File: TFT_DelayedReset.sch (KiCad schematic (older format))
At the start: 14 parts, among them Q2 MMBT3904, U3 MCP601-xOT, U4 LM555xM, U5 MCP1416, U6 MCP1415

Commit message: Swapped LM555 with MIC1555
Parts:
- removed U4: LM555xM, Package_SO:SOIC-8_3.9x4.9mm_P1.27mm, symbol Timer:LM555xM
- added U4: MIC1555-YM5, Package_TO_SOT_SMD:SOT-23-5_HandSoldering, symbol MIC155x:MIC1555-YM5
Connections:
- wire segments 57 -> 54
- no-connect marks 1 -> 0
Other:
- moved on the sheet: U3
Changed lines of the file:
@@
 L Amplifier_Operational:MCP601-xOT U?
 U 1 1 5F17E98F
-P 2275 4125
+P 2275 3350
 AR Path="/5F02F4E9/5F17E98F" Ref="U?"  Part="1"
 AR Path="/5F02F4E9/5F1755C4/5F17E98F" Ref="U3"  Part="1"
-F 0 "U3" H 1800 4625 50  0000 L CNN
-F 1 "MCP601-xOT" H 1575 4500 50  0000 L CNN
-F 2 "Package_TO_SOT_SMD:SOT-23-5" H 2175 3925 50  0001 L CNN
-F 3 "http://ww1.microchip.com/downloads/en/DeviceDoc/21314g.pdf" H 2275 4325 50  0001 C CNN
-	1    2275 4125
-	1    0    0    -1
-$EndComp
-Wire Wire Line
-	2175 4425 2175 4475
-Text HLabel 2175 4475 3    50   Input ~ 0
-TFTRST_GND
-Wire Wire Line
-	2175 3825 2175 3450
-Text HLabel 2175 3450 1    50   Input ~ 0
-TFTRST_5V
-Wire Wire Line
-	1975 4025 1625 4025
-Wire Wire Line
-	1975 4225 1600 4225
-Wire Wire Line
-	1600 4225 1600 5200
-Wire Wire Line
-	1600 5200 2725 5200
-Wire Wire Line
-	2725 5200 2725 4125
-Wire Wire Line
-	2725 4125 2575 4125
-$Comp
-L Timer:LM555xM U?
-U 1 1 5F17E9A0
-P 4250 4325
-AR Path="/5F02F4E9/5F17E9A0" Ref="U?"  Part="1"
-AR Path="/5F02F4E9/5F1755C4/5F17E9A0" Ref="U4"  Part="1"
-F 0 "U4" H 3900 4825 50  0000 C CNN
-F 1 "LM555xM" H 3900 4725 50  0000 C CNN
-F 2 "Package_SO:SOIC-8_3.9x4.9mm_P1.27mm" H 5100 3925 50  0001 C CNN
-F 3 "http://www.ti.com/lit/ds/symlink/lm555.pdf" H 5100 3925 50  0001 C CNN
-	1    4250 4325
-	1    0    0    -1
-$EndComp
-Wire Wire Line
-	3750 4125 2725 4125
-Connection ~ 2725 4125
-Wire Wire Line
-	4250 3925 4250 3425
-Wire Wire Line
-	4250 4725 4250 4775
-Wire Wire Line
-	4750 4325 4900 4325
-Wire Wire Line
-	4900 4325 4900 4525
-Wire Wire Line
-	4900 4525 4750 4525
-$Comp
-L Device:R R?
-U 1 1 5F17E9AF
-P 5500 4325
-AR Path="/5F02F4E9/5F17E9AF" Ref="R?"  Part="1"
-AR Path="/5F02F4E9/5F1755C4/5F17E9AF" Ref="R5"  Part="1"
-F 0 "R5" V 5400 4200 50  0000 L CNN
-F 1 "1Meg" V 5400 4325 50  0000 L CNN
-F 2 "Resistor_SMD:R_0805_2012Metric_Pad1.15x1.40mm_HandSolder" V 5430 4325 50  0001 C CNN
-F 3 "~" H 5500 4325 50  0001 C CNN
-	1    5500 4325
-	0    1    1    0
-$EndComp
-$Comp
-L Device:C C?
-U 1 1 5F17E9B5
-P 5500 4525
-AR Path="/5F02F4E9/5F17E9B5" Ref="C?"  Part="1"
-AR Path="/5F02F4E9/5F1755C4/5F17E9B5" Ref="C7"  Part="1"
-F 0 "C7" V 5650 4425 50  0000 C CNN
-F 1 "2.2uF" V 5650 4650 50  0000 C CNN
-F 2 "Capacitor_SMD:C_0805_2012Metric_Pad1.15x1.40mm_HandSolder" H 5538 4375 50  0001 C CNN
-F 3 "~" H 5500 4525 50  0001 C CNN
-	1    5500 4525
-	0    1    1    0
-$EndComp
-Connection ~ 4900 4525
-Wire Wire Line
-	5825 4675 5825 4525
-Wire Wire Line
-	5825 4325 5650 4325
-NoConn ~ 3750 4325
-Wire Wire Line
-	3500 4525 3750 4525
-Wire Wire Line
-	4900 4325 5350 4325
-Wire Wire Line
-	4750 4125 5250 4125
-Wire Wire Line
-	5825 4325 5825 4100
-Wire Wire Line
-	5250 4125 5250 3250
-Connection ~ 4900 4325
-Wire Wire Line
-	5825 4525 5650 4525
-Wire Wire Line
-	4900 4525 5350 4525
+F 0 "U3" H 1800 3850 50  0000 L CNN
+F 1 "MCP601-xOT" H 1575 3725 50  0000 L CNN
+F 2 "Package_TO_SOT_SMD:SOT-23-5" H 2175 3150 50  0001 L CNN
+F 3 "http://ww1.microchip.com/downloads/en/DeviceDoc/21314g.pdf" H 2275 3550 50  0001 C CNN
+	1    2275 3350
+	1    0    0    -1
+$EndComp
+Wire Wire Line
+	2175 3650 2175 3700
+Text HLabel 2175 3700 3    50   Input ~ 0
+TFTRST_GND
+Wire Wire Line
+	2175 3050 2175 2675
+Text HLabel 2175 2675 1    50   Input ~ 0
+TFTRST_5V
+Wire Wire Line
+	1975 3250 1625 3250
+Wire Wire Line
+	1975 3450 1600 3450
+Wire Wire Line
+	1600 3450 1600 4425
+Wire Wire Line
+	1600 4425 2725 4425
+Wire Wire Line
+	2725 4425 2725 3350
+Wire Wire Line
+	2725 3350 2575 3350
 $Comp
 L Transistor_BJT:MMBT3904 Q2
@@
 	8425 4100 6225 4100
 Wire Wire Line
-	6225 4100 6225 3250
-Wire Wire Line
 	9125 4100 10175 4100
 Wire Wire Line
@@
 Text HLabel 10550 2975 2    50   Input ~ 0
 TFT_VDD_OUT
-Text HLabel 1625 4025 0    50   Input ~ 0
+Text HLabel 1625 3250 0    50   Input ~ 0
 NRST_IN
-Text HLabel 4250 3425 1    50   Input ~ 0
-TFTRST_5V
 Text HLabel 7425 1600 1    50   Input ~ 0
 TFTRST_5V
@@
 Text HLabel 8725 3600 1    50   Input ~ 0
 TFTRST_5V
-Text HLabel 5825 4100 1    50   Input ~ 0
-TFTRST_5V
 Wire Wire Line
 	8425 2050 8125 2050
 Wire Wire Line
 	8125 2050 8125 2200
-Text HLabel 3500 4525 0    50   Input ~ 0
-TFTRST_5V
-Text HLabel 4250 4775 3    50   Input ~ 0
-TFTRST_GND
-Text HLabel 5825 4675 3    50   Input ~ 0
-TFTRST_GND
 Text HLabel 8725 4600 3    50   Input ~ 0
 TFTRST_GND
@@
 Wire Wire Line
 	7775 5550 7775 5475
-Wire Wire Line
-	5250 3250 6225 3250
-Connection ~ 6225 3250
-Wire Wire Line
-	6225 3250 6225 2500
+$Comp
+L MIC155x:MIC1555-YM5 U4
+U 1 1 5F11D4BD
+P 4125 3350
+F 0 "U4" H 4125 3765 50  0000 C CNN
+F 1 "MIC1555-YM5" H 4125 3674 50  0000 C CNN
+F 2 "Package_TO_SOT_SMD:SOT-23-5_HandSoldering" H 4025 3350 50  0001 C CNN
+F 3 "http://ww1.microchip.com/downloads/en/DeviceDoc/mic1555.pdf" H 4025 3350 50  0001 C CNN
+	1    4125 3350
+	1    0    0    -1
+$EndComp
+Wire Wire Line
+	3775 3200 3500 3200
+Wire Wire Line
+	3500 3200 3500 3075
+Text HLabel 3500 3075 1    50   Input ~ 0
+TFTRST_5V
+Text HLabel 3500 4150 3    50   Input ~ 0
+TFTRST_GND
+Wire Wire Line
+	3775 3500 3500 3500
+Wire Wire Line
+	3500 3500 3500 4150
+$Comp
+L Device:C C?
+U 1 1 5F127B66
+P 5050 3800
+AR Path="/5F02F4E9/5F127B66" Ref="C?"  Part="1"
+AR Path="/5F02F4E9/5F1755C4/5F127B66" Ref="C7"  Part="1"
+F 0 "C7" H 5275 3775 50  0000 C CNN
+F 1 "2.2uF" H 5275 3875 50  0000 C CNN
+F 2 "Capacitor_SMD:C_0805_2012Metric_Pad1.15x1.40mm_HandSolder" H 5088 3650 50  0001 C CNN
+F 3 "~" H 5050 3800 50  0001 C CNN
+	1    5050 3800
+	-1   0    0    1
+$EndComp
+$Comp
+L Device:R R?
+U 1 1 5F128999
+P 5050 3200
+AR Path="/5F02F4E9/5F128999" Ref="R?"  Part="1"
+AR Path="/5F02F4E9/5F1755C4/5F128999" Ref="R5"  Part="1"
+F 0 "R5" V 4950 3075 50  0000 L CNN
+F 1 "1Meg" V 4950 3200 50  0000 L CNN
+F 2 "Resistor_SMD:R_0805_2012Metric_Pad1.15x1.40mm_HandSolder" V 4980 3200 50  0001 C CNN
+F 3 "~" H 5050 3200 50  0001 C CNN
+	1    5050 3200
+	-1   0    0    1
+$EndComp
+Wire Wire Line
+	4475 3200 4675 3200
+Wire Wire Line
+	4675 3200 4675 2500
+Wire Wire Line
+	4675 2500 5050 2500
+Wire Wire Line
+	4475 3500 5050 3500
+Wire Wire Line
+	5050 3500 5050 3350
+Wire Wire Line
+	5050 3050 5050 2500
+Connection ~ 5050 2500
+Wire Wire Line
+	5050 2500 6225 2500
+Wire Wire Line
+	5050 3650 5050 3500
+Connection ~ 5050 3500
+Wire Wire Line
+	3775 3350 2725 3350
+Connection ~ 2725 3350
+Connection ~ 6225 2500
+Wire Wire Line
+	6225 2500 6225 4100
+Text HLabel 5050 4100 3    50   Input ~ 0
+TFTRST_GND
+Wire Wire Line
+	5050 3950 5050 4100
 $EndSCHEMATC

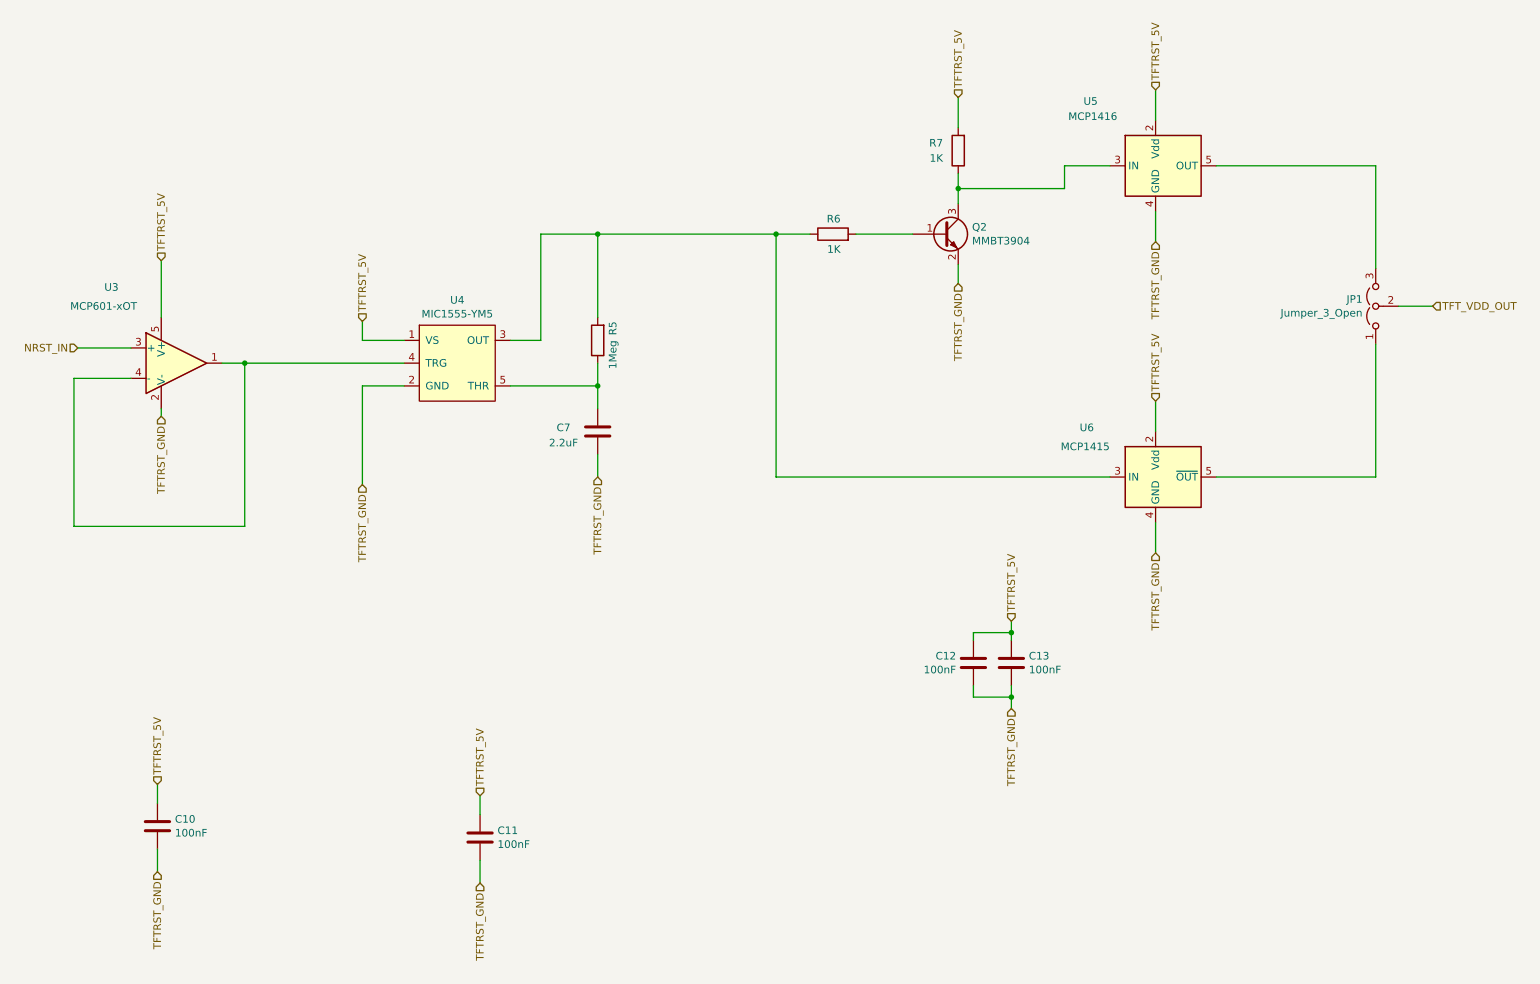
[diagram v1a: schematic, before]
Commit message: updated hw
- added SMBUS address HW 
- Changed Isolated DC Module to TI SimpleSwitcher IC
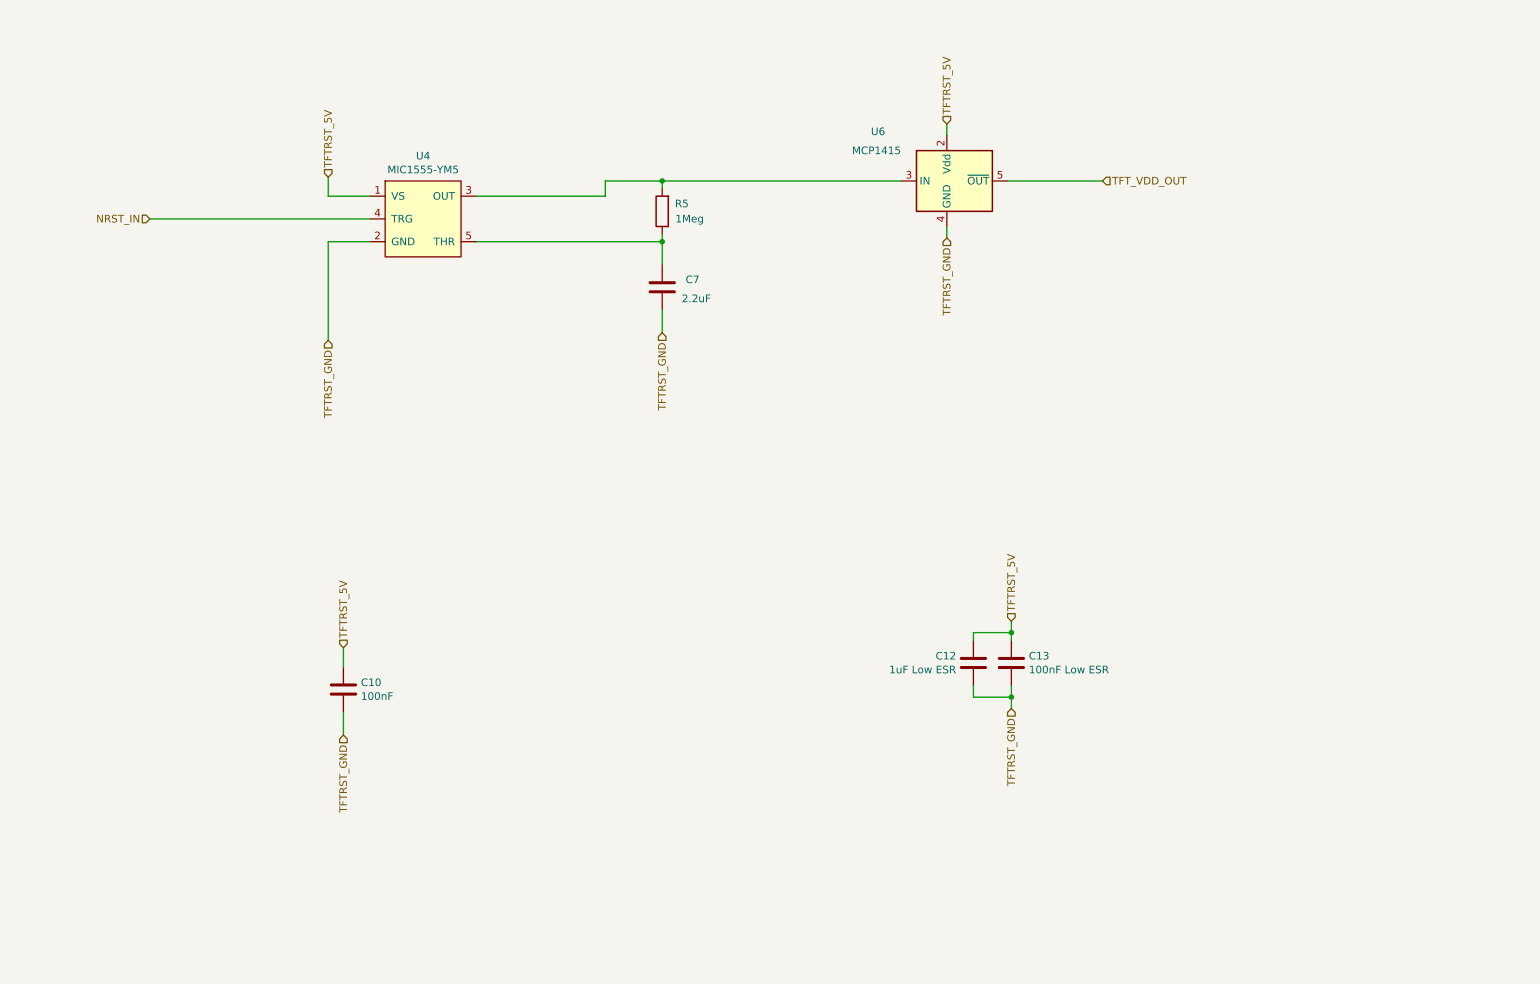
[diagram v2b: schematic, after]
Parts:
- removed C11: 100nF, Capacitor_SMD:C_0805_2012Metric_Pad1.15x1.40mm_HandSolder, symbol Device:C
- removed JP1: Jumper_3_Open, Jumper:SolderJumper-3_P1.3mm_Open_Pad1.0x1.5mm, symbol Jumper:Jumper_3_Open
- removed Q2: MMBT3904, Package_TO_SOT_SMD:SOT-23, symbol Transistor_BJT:MMBT3904
- removed R6, R7: 1K, Resistor_SMD:R_0805_2012Metric_Pad1.15x1.40mm_HandSolder, symbol Device:R
- removed U3: MCP601-xOT, Package_TO_SOT_SMD:SOT-23-5, symbol Amplifier_Operational:MCP601-xOT
- removed U5: MCP1416, Package_TO_SOT_SMD:SOT-23-5, symbol Driver_FET:MCP1416
- C12: value 100nF -> 1uF Low ESR
- C13: value 100nF -> 100nF Low ESR
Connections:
- net NRST_IN: now also U4.4 (TRG)
- net TFT_VDD_OUT: now also U6.5 (~OUT)
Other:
- moved on the sheet: C10, C7, R5, U4, U6

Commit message: Completed RevA
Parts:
- added TP10, TP7, TP8, TP9: TestPoint, TestPoint:TestPoint_Pad_1.0x1.0mm, symbol Connector:TestPoint
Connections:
- net NRST_IN: now also TP9.1
- net TFT_VDD_OUT: now also TP7.1
- net TFTRST_GND renamed GNDS
- net GNDS: now also TP10.1, TP8.1
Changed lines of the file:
@@
 	7350 1850 7350 1775
 Wire Wire Line
-	7350 2525 7350 2450
+	7350 3025 7350 2450
 Text HLabel 8375 2150 2    50   Input ~ 0
 TFT_VDD_OUT
@@
 Text HLabel 7350 1775 1    50   Input ~ 0
 TFTRST_5V
-Text HLabel 7350 2525 3    50   Input ~ 0
-TFTRST_GND
 $Comp
 L Device:C C10
@@
 Wire Wire Line
 	3375 5225 3375 5350
-Text HLabel 3375 5800 3    50   Input ~ 0
-TFTRST_GND
 Wire Wire Line
 	3375 5800 3375 5650
@@
 Wire Wire Line
 	7775 5050 7775 5125
-Text HLabel 7775 5625 3    50   Input ~ 0
-TFTRST_GND
 Wire Wire Line
 	7775 5625 7775 5550
@@
 Text HLabel 3275 2125 1    50   Input ~ 0
 TFTRST_5V
-Text HLabel 3275 3200 3    50   Input ~ 0
-TFTRST_GND
 Wire Wire Line
 	3550 2550 3275 2550
 Wire Wire Line
-	3275 2550 3275 3200
+	3275 2550 3275 2975
 $Comp
 L Device:C C?
@@
 	5475 2700 5475 2550
 Connection ~ 5475 2550
-Text HLabel 5475 3150 3    50   Input ~ 0
-TFTRST_GND
 Wire Wire Line
 	5475 3000 5475 3150
 Wire Wire Line
-	3550 2400 2100 2400
-Wire Wire Line
-	7750 2150 8375 2150
+	3550 2400 2425 2400
+Wire Wire Line
+	7750 2150 8150 2150
 Wire Wire Line
 	5475 2150 7050 2150
@@
 EndData
 $EndBitmap
+$Comp
+L Connector:TestPoint TP?
+U 1 1 5F1B32BC
+P 8150 1925
+AR Path="/5F02F4E9/5F1B32BC" Ref="TP?"  Part="1"
+AR Path="/5EFF0F4B/5F1B32BC" Ref="TP?"  Part="1"
+AR Path="/5F02F4E9/5F1755C4/5F1B32BC" Ref="TP7"  Part="1"
+F 0 "TP7" H 8208 2043 50  0000 L CNN
+F 1 "TestPoint" H 8208 1952 50  0000 L CNN
+F 2 "TestPoint:TestPoint_Pad_1.0x1.0mm" H 8350 1925 50  0001 C CNN
+F 3 "~" H 8350 1925 50  0001 C CNN
+	1    8150 1925
+	1    0    0    -1
+$EndComp
+Wire Wire Line
+	8150 1925 8150 2150
+$Comp
+L Connector:TestPoint TP?
+U 1 1 5F1B3956
+P 8150 2725
+AR Path="/5F02F4E9/5F1B3956" Ref="TP?"  Part="1"
+AR Path="/5EFF0F4B/5F1B3956" Ref="TP?"  Part="1"
+AR Path="/5F02F4E9/5F1755C4/5F1B3956" Ref="TP8"  Part="1"
+F 0 "TP8" H 8208 2843 50  0000 L CNN
+F 1 "TestPoint" H 8208 2752 50  0000 L CNN
+F 2 "TestPoint:TestPoint_Pad_1.0x1.0mm" H 8350 2725 50  0001 C CNN
+F 3 "~" H 8350 2725 50  0001 C CNN
+	1    8150 2725
+	1    0    0    -1
+$EndComp
+Wire Wire Line
+	8150 2725 8150 2950
+Connection ~ 8150 2150
+Wire Wire Line
+	8150 2150 8375 2150
+$Comp
+L power:GNDS #PWR0103
+U 1 1 5F1BB0D4
+P 8150 2950
+F 0 "#PWR0103" H 8150 2700 50  0001 C CNN
+F 1 "GNDS" H 8155 2777 50  0000 C CNN
+F 2 "" H 8150 2950 50  0001 C CNN
+F 3 "" H 8150 2950 50  0001 C CNN
+	1    8150 2950
+	1    0    0    -1
+$EndComp
+$Comp
+L power:GNDS #PWR0104
+U 1 1 5F1BB592
+P 7350 3025
+F 0 "#PWR0104" H 7350 2775 50  0001 C CNN
+F 1 "GNDS" H 7355 2852 50  0000 C CNN
+F 2 "" H 7350 3025 50  0001 C CNN
+F 3 "" H 7350 3025 50  0001 C CNN
+	1    7350 3025
+	1    0    0    -1
+$EndComp
+$Comp
+L power:GNDS #PWR0105
+U 1 1 5F1BB8A6
+P 5475 3150
+F 0 "#PWR0105" H 5475 2900 50  0001 C CNN
+F 1 "GNDS" H 5480 2977 50  0000 C CNN
+F 2 "" H 5475 3150 50  0001 C CNN
+F 3 "" H 5475 3150 50  0001 C CNN
+	1    5475 3150
+	1    0    0    -1
+$EndComp
+$Comp
+L power:GNDS #PWR0106
+U 1 1 5F1BC048
+P 3275 3200
+F 0 "#PWR0106" H 3275 2950 50  0001 C CNN
+F 1 "GNDS" H 3280 3027 50  0000 C CNN
+F 2 "" H 3275 3200 50  0001 C CNN
+F 3 "" H 3275 3200 50  0001 C CNN
+	1    3275 3200
+	1    0    0    -1
+$EndComp
+$Comp
+L power:GNDS #PWR0107
+U 1 1 5F1BC800
+P 3375 5800
+F 0 "#PWR0107" H 3375 5550 50  0001 C CNN
+F 1 "GNDS" H 3380 5627 50  0000 C CNN
+F 2 "" H 3375 5800 50  0001 C CNN
+F 3 "" H 3375 5800 50  0001 C CNN
+	1    3375 5800
+	1    0    0    -1
+$EndComp
+$Comp
+L power:GNDS #PWR0108
+U 1 1 5F1BCEFD
+P 7775 5625
+F 0 "#PWR0108" H 7775 5375 50  0001 C CNN
+F 1 "GNDS" H 7780 5452 50  0000 C CNN
+F 2 "" H 7775 5625 50  0001 C CNN
+F 3 "" H 7775 5625 50  0001 C CNN
+	1    7775 5625
+	1    0    0    -1
+$EndComp
+$Comp
+L Connector:TestPoint TP?
+U 1 1 5F1CCF1D
+P 2425 2175
+AR Path="/5F02F4E9/5F1CCF1D" Ref="TP?"  Part="1"
+AR Path="/5EFF0F4B/5F1CCF1D" Ref="TP?"  Part="1"
+AR Path="/5F02F4E9/5F1755C4/5F1CCF1D" Ref="TP9"  Part="1"
+F 0 "TP9" H 2483 2293 50  0000 L CNN
+F 1 "TestPoint" H 2483 2202 50  0000 L CNN
+F 2 "TestPoint:TestPoint_Pad_1.0x1.0mm" H 2625 2175 50  0001 C CNN
+F 3 "~" H 2625 2175 50  0001 C CNN
+	1    2425 2175
+	1    0    0    -1
+$EndComp
+Wire Wire Line
+	2425 2175 2425 2400
+Connection ~ 2425 2400
+Wire Wire Line
+	2425 2400 2100 2400
+$Comp
+L Connector:TestPoint TP?
+U 1 1 5F1CD729
+P 2425 2750
+AR Path="/5F02F4E9/5F1CD729" Ref="TP?"  Part="1"
+AR Path="/5EFF0F4B/5F1CD729" Ref="TP?"  Part="1"
+AR Path="/5F02F4E9/5F1755C4/5F1CD729" Ref="TP10"  Part="1"
+F 0 "TP10" H 2483 2868 50  0000 L CNN
+F 1 "TestPoint" H 2483 2777 50  0000 L CNN
+F 2 "TestPoint:TestPoint_Pad_1.0x1.0mm" H 2625 2750 50  0001 C CNN
+F 3 "~" H 2625 2750 50  0001 C CNN
+	1    2425 2750
+	1    0    0    -1
+$EndComp
+Wire Wire Line
+	2425 2750 2425 2975
+Wire Wire Line
+	2425 2975 3275 2975
+Connection ~ 3275 2975
+Wire Wire Line
+	3275 2975 3275 3200
 $EndSCHEMATC

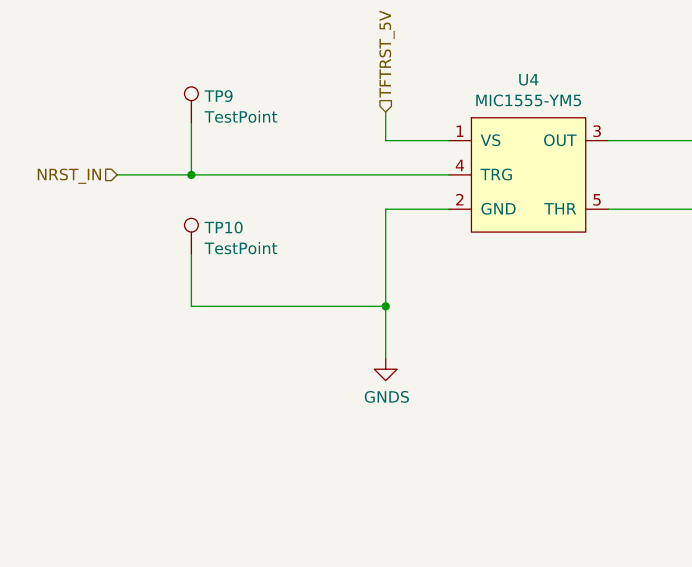
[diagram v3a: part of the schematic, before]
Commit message: Corrected Pin numbering errors :)
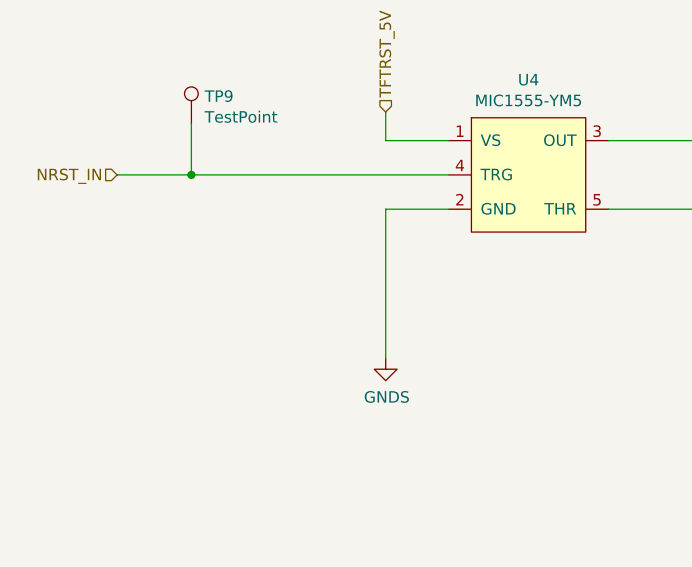
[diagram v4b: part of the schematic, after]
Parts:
- removed TP10: TestPoint, TestPoint:TestPoint_Pad_1.0x1.0mm, symbol Connector:TestPoint
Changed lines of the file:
@@
 Wire Wire Line
 	3550 2550 3275 2550
-Wire Wire Line
-	3275 2550 3275 2975
 $Comp
 L Device:C C?
@@
 Wire Wire Line
 	2425 2400 2100 2400
-$Comp
-L Connector:TestPoint TP?
-U 1 1 5F1CD729
-P 2425 2750
-AR Path="/5F02F4E9/5F1CD729" Ref="TP?"  Part="1"
-AR Path="/5EFF0F4B/5F1CD729" Ref="TP?"  Part="1"
-AR Path="/5F02F4E9/5F1755C4/5F1CD729" Ref="TP10"  Part="1"
-F 0 "TP10" H 2483 2868 50  0000 L CNN
-F 1 "TestPoint" H 2483 2777 50  0000 L CNN
-F 2 "TestPoint:TestPoint_Pad_1.0x1.0mm" H 2625 2750 50  0001 C CNN
-F 3 "~" H 2625 2750 50  0001 C CNN
-	1    2425 2750
-	1    0    0    -1
-$EndComp
 Wire Wire Line
-	2425 2750 2425 2975
-Wire Wire Line
-	2425 2975 3275 2975
-Connection ~ 3275 2975
-Wire Wire Line
-	3275 2975 3275 3200
+	3275 2550 3275 3200
 $EndSCHEMATC
